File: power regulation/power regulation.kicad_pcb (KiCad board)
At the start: 4 copper layers, 200 x 100 mm, 89 parts, among them J1 Conn_01x02_Pin, J2 Conn_01x02_Pin, J3 Conn_01x02_Pin, M1 TO-236AB_SOT23_NEX, M2 TO-236AB_SOT23_NEX, U1 LT8640SEV_PBF, U2 LT8640SEV_PBF, U3 LT8619EDD-TRPBF

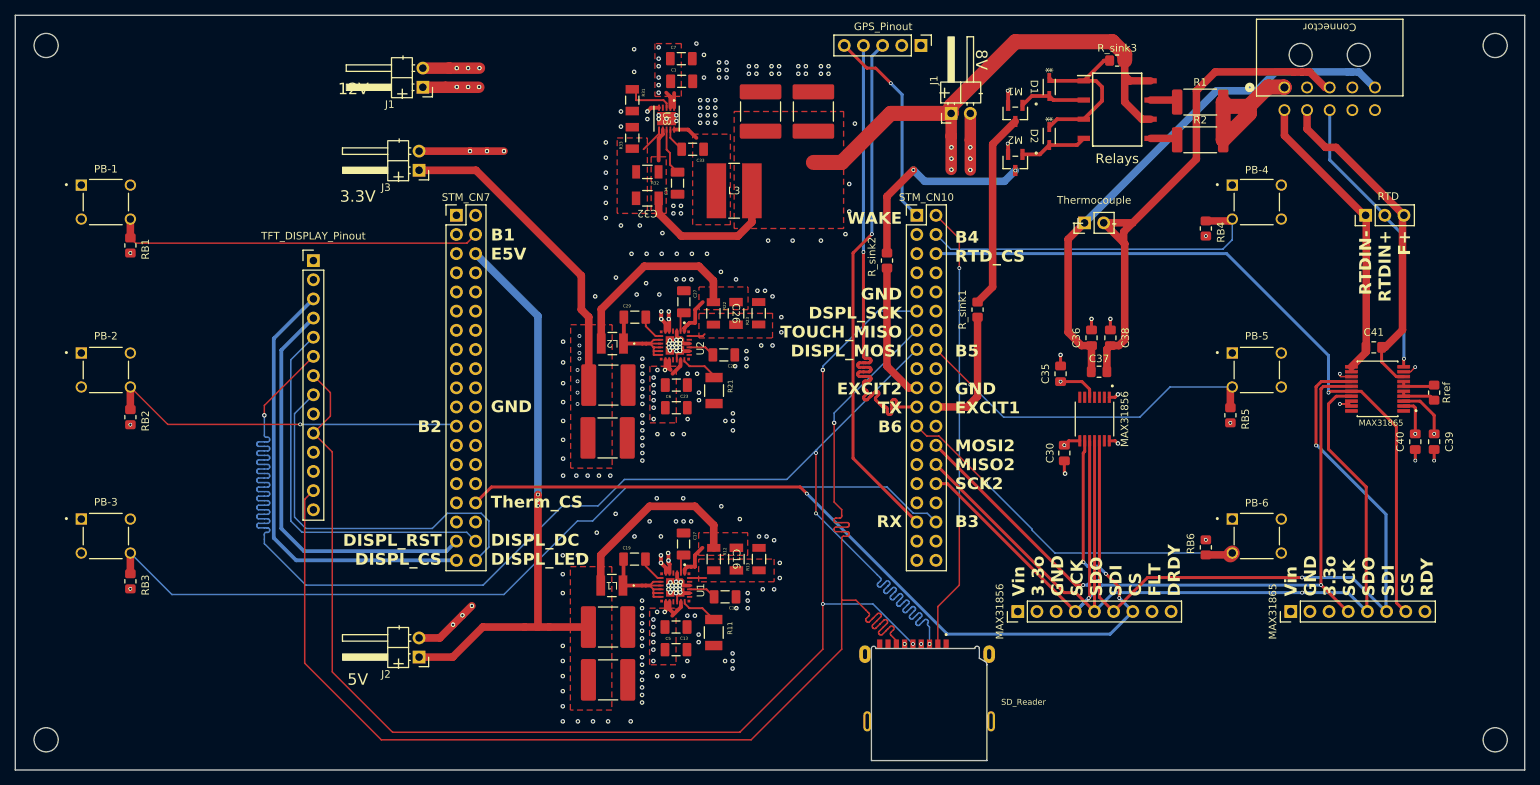
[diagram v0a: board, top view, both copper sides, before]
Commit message: resize button spacing for screen and moved screen headers to center.
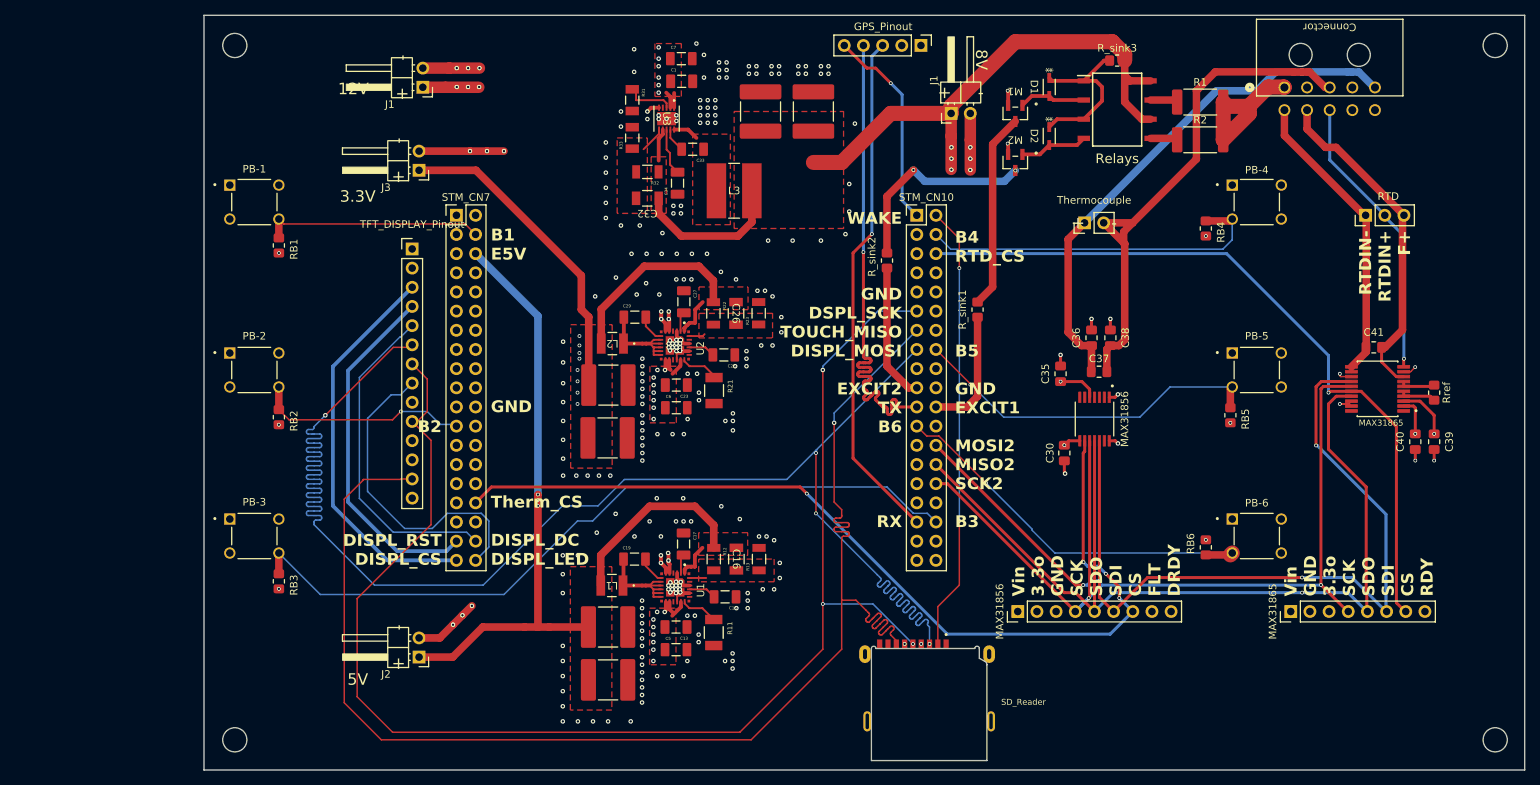
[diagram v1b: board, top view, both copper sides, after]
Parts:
- moved REF** 25.0 mm to (73.5, 138.0)
- moved REF** 25.0 mm to (73.5, 46.0)
- moved PB-1 19.7 mm to (76.1, 66.8)
- moved PB-2 19.7 mm to (76.1, 89.0)
- moved PB-3 19.7 mm to (76.1, 111.0)
- moved RB1 19.7 mm to (79.3, 72.5)
- moved RB2 19.7 mm to (79.3, 95.2)
- moved RB3 19.7 mm to (79.3, 117.0)
- moved TFT_DISPLAY_Pinout 13.2 mm to (97.0, 73.0)
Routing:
- net B2: track 48.3 -> 28.3 mm
- net B3: track 119.6 -> 99.9 mm
- net B1: track 49.0 -> 29.4 mm
- net DISPL_LED: track 50.8 -> 42.8 mm
- net DISPL_RST: track 54.6 -> 47.0 mm
- net DISPL_DC: track 51.2 -> 43.6 mm
- net DISPL_CS: track 59.3 -> 52.7 mm
- net TOUCH_MISO: track 178.1 -> 184.4 mm
- net DISPL_SCK: track 182.1 -> 186.6 mm
- net DISPL_MOSI: track 208.6 -> 210.9 mm
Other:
- board size 200 x 100 mm -> 175 x 100 mm

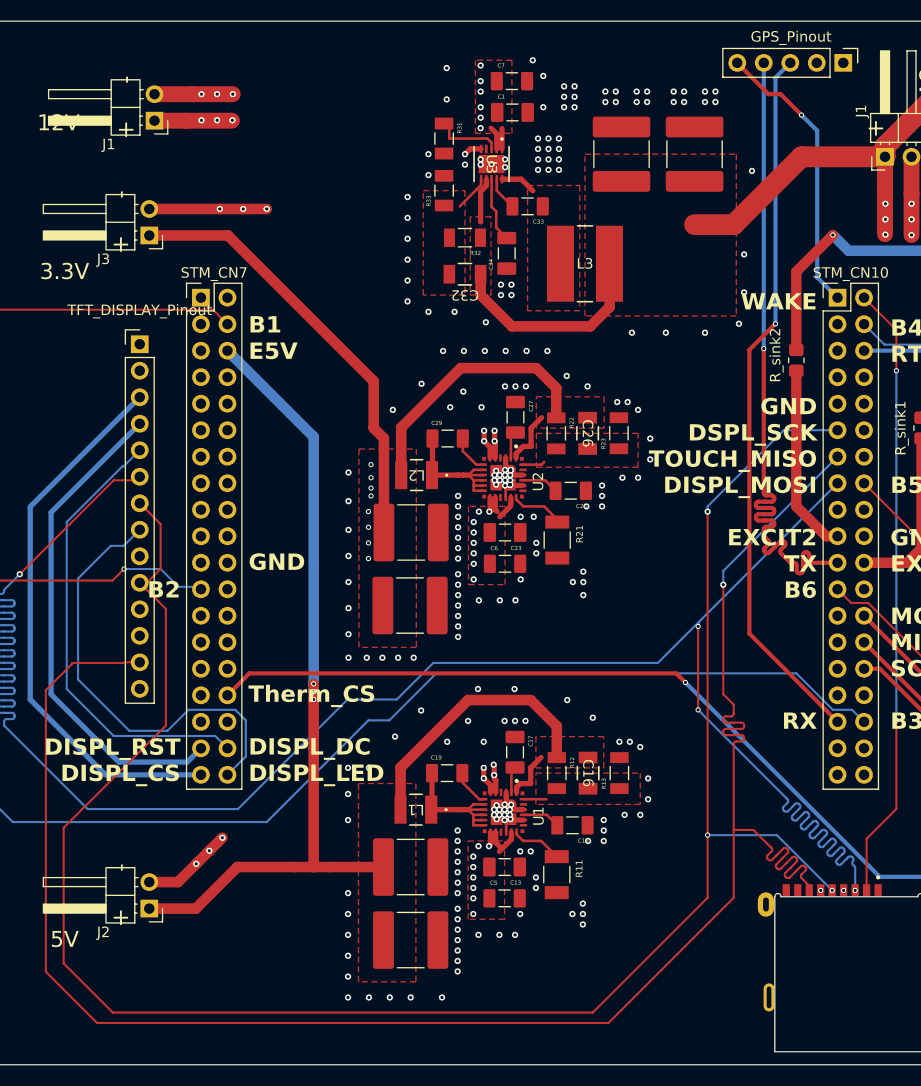
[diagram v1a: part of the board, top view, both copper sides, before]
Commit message: Move GPS headers
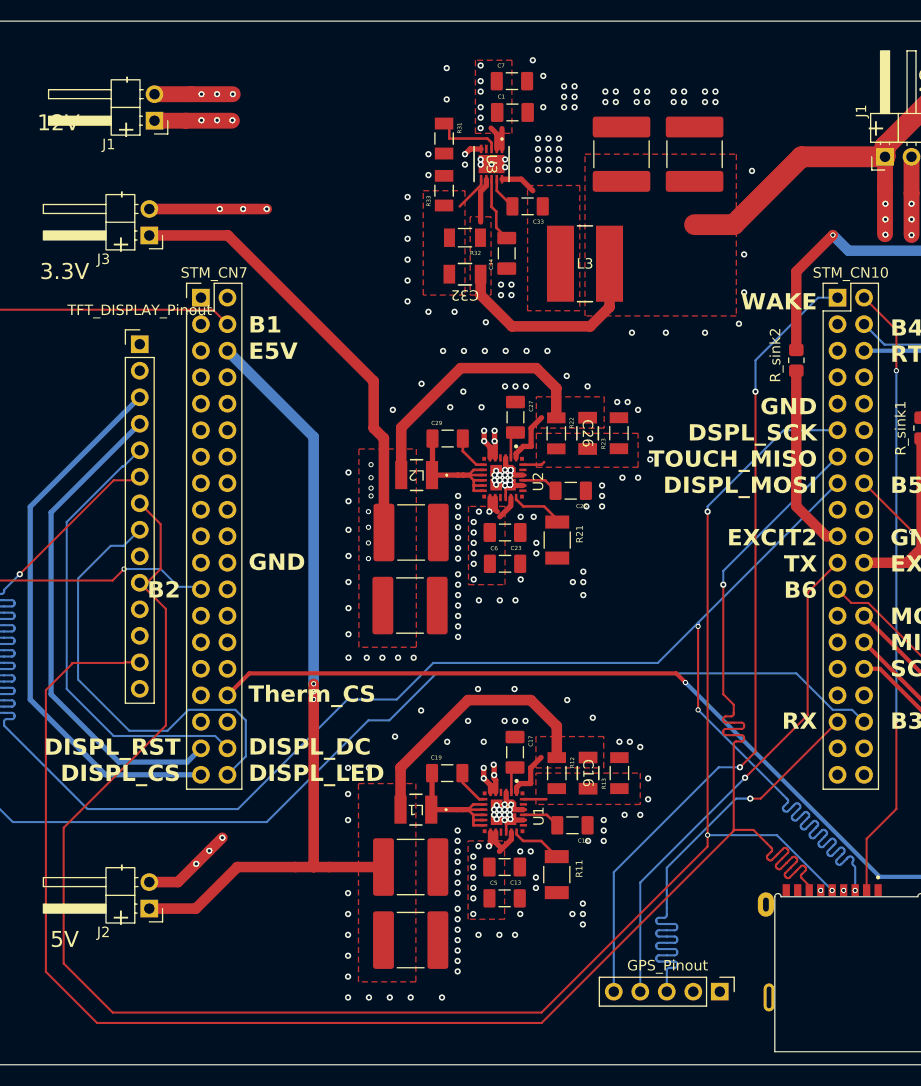
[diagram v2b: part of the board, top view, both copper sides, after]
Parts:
- moved GPS_Pinout 89.8 mm to (152.6, 135.0)
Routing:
- net WAKE: track 27.2 -> 77.7 mm, vias 1 -> 2
- net RX: track 68.3 -> 48.0 mm
- net TX: track 67.8 -> 48.9 mm
- net TOUCH_MISO: track 184.4 -> 180.7 mm
- net DISPL_SCK: track 186.6 -> 183.7 mm
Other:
- board text added: "STM_CN10"
- board text added: "STM_CN7"

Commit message: Add outlines for external MAX modules
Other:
- board text added: "-> STM_Programmer <-"
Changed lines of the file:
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@@
 	)
 	(gr_rect
-		(start 207.4125 70.5)
-		(end 237.4125 125.5)
+		(start 209.5 95)
+		(end 235 123)
 		(stroke
 			(width 0.1)
-			(type default)
-		)
-		(fill no)
-		(layer "B.SilkS")
-	)
-	(gr_rect
-		(start 173.9125 71.5)
-		(end 200.9125 126)
+			(type solid)
+		)
+		(fill no)
+		(layer "B.SilkS")
+	)
+	(gr_rect
+		(start 175 101)
+		(end 200 123)
 		(stroke
 			(width 0.1)
-			(type default)
+			(type solid)
 		)
 		(fill no)
@@
 		)
 	)
+	(gr_text "-> STM_Programmer <-"
+		(at 133.5 55.5 0)
+		(layer "B.SilkS")
+		(effects
+			(font
+				(size 2 2)
+				(thickness 0.25)
+			)
+			(justify bottom mirror)
+		)
+	)
 	(gr_text "Vin\nGND\n3.3o\nSCK\nSDO\nSDI\nCS\nRDY"
 		(at 232.4125 119 90)
@@
 	)
 	(gr_text "MAX31865"
-		(at 210.9125 121 90)
+		(at 208.5 119 90)
 		(layer "B.SilkS")
 		(effects
@@
 	)
 	(gr_text "MAX31856"
-		(at 174.9125 121 90)
-		(layer "B.SilkS")
-		(effects
+		(at 174 119.5 90)
+		(layer "B.SilkS")
+		(effects

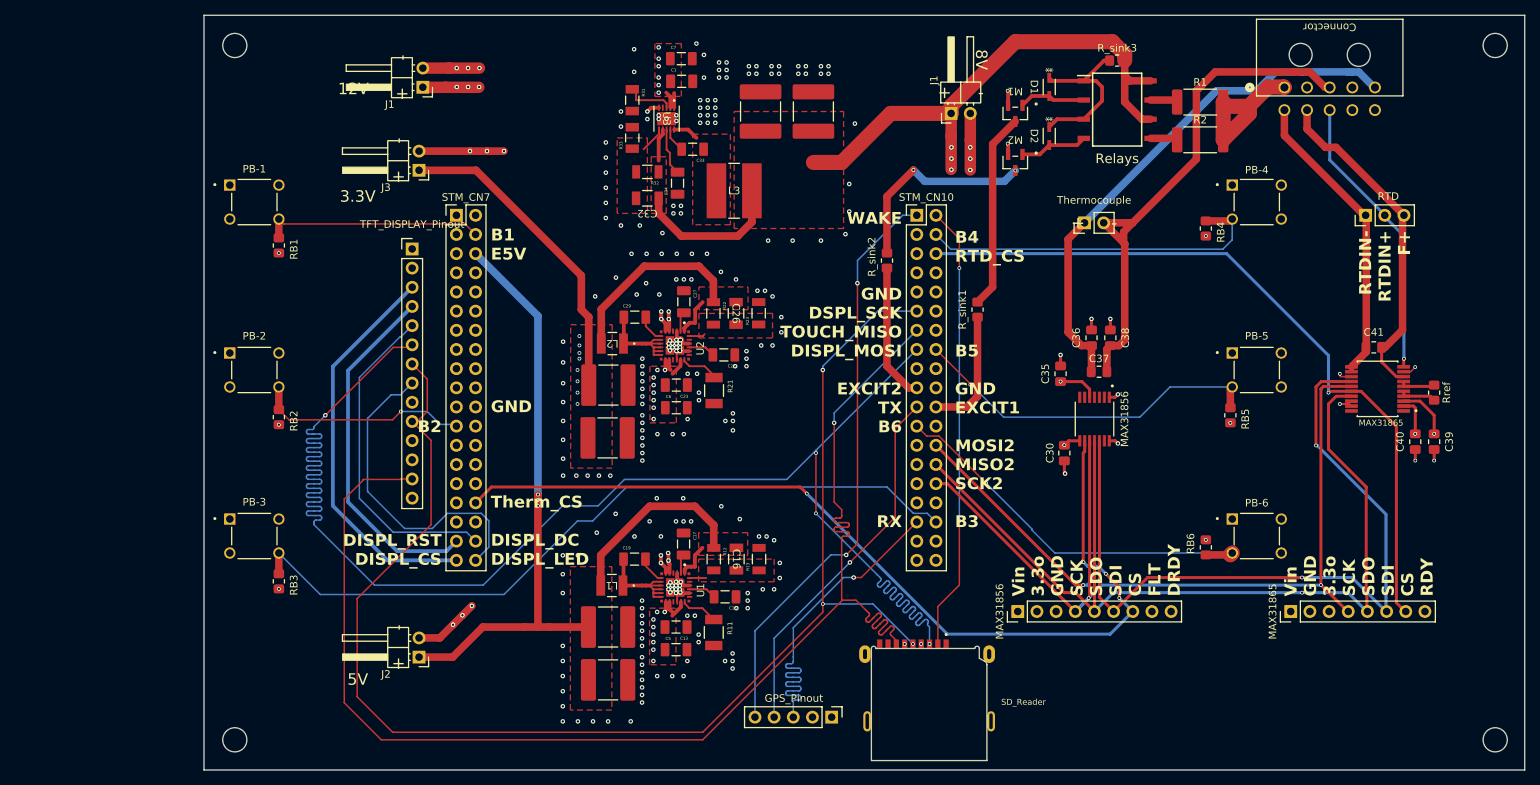
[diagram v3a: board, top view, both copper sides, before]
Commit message: Flip Maxx modules so they can be mounted upsidown on the bottom of the board. I also made some changes to silk screens and vias to remove a bunch of wranings.
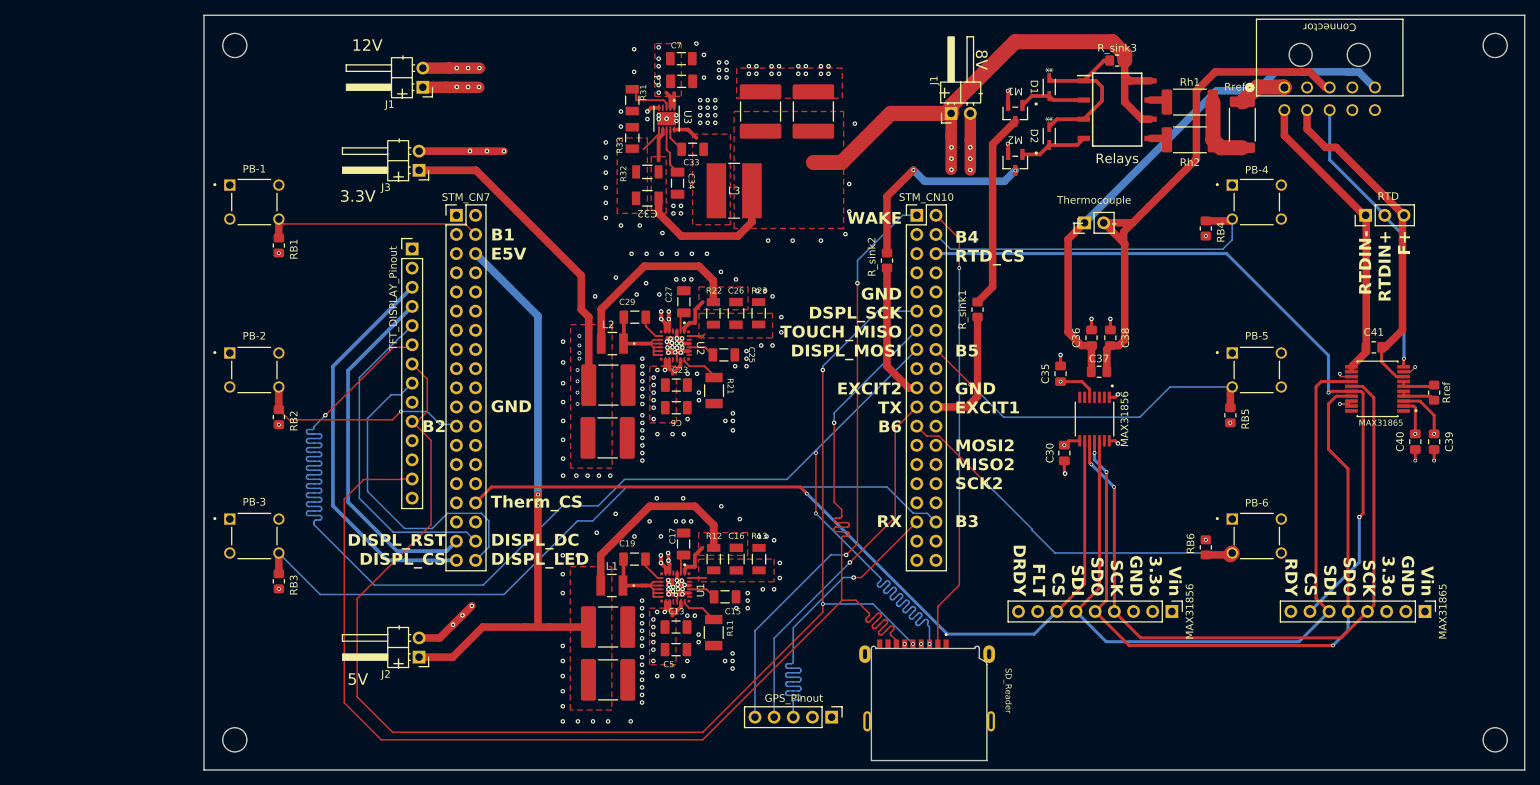
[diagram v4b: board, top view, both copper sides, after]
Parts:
- added Rref: R_2512_6332Metric_Pad1.40x3.35mm_HandSolder, Resistor_SMD:R_2512_6332Metric_Pad1.40x3.35mm_HandSolder, F.Cu at (207.0, 56.5)
- moved MAX31856 20.4 mm to (197.7, 121.0), turned to -90 degrees
- moved MAX31865 17.8 mm to (231.2, 121.0), turned to -90 degrees
- moved Rh1 1.36 mm to (200.1, 53.5)
- moved Rh2 1.36 mm to (200.1, 58.5)
- renumbered R1 to Rh1, R2 to Rh2
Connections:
- Rh1 pad 2: Heater+ -> HeaterPre
- Rh2 pad 2: Heater+ -> HeaterPre
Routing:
- net MAX_SDI: track 131.5 -> 96.2 mm, vias 4 -> 0
- net MAX_SDO: track 122.9 -> 94.7 mm, vias 2 -> 3
- net MAX_SCK: track 118.1 -> 92.7 mm
- net Heater+: track 20.5 -> 6.41 mm
- net Therm_CS: track 123.6 -> 111.4 mm, vias 4 -> 1
- net HeaterPre: track 0.00 -> 9.33 mm
- net SSRout-2: track 3.60 -> 2.24 mm
- net SSRout-1: track 3.64 -> 2.27 mm
- net RTD_CS: track 98.5 -> 99.1 mm, vias 1 -> 2
- net GND: track 69.0 -> 69.1 mm, vias 256 -> 250

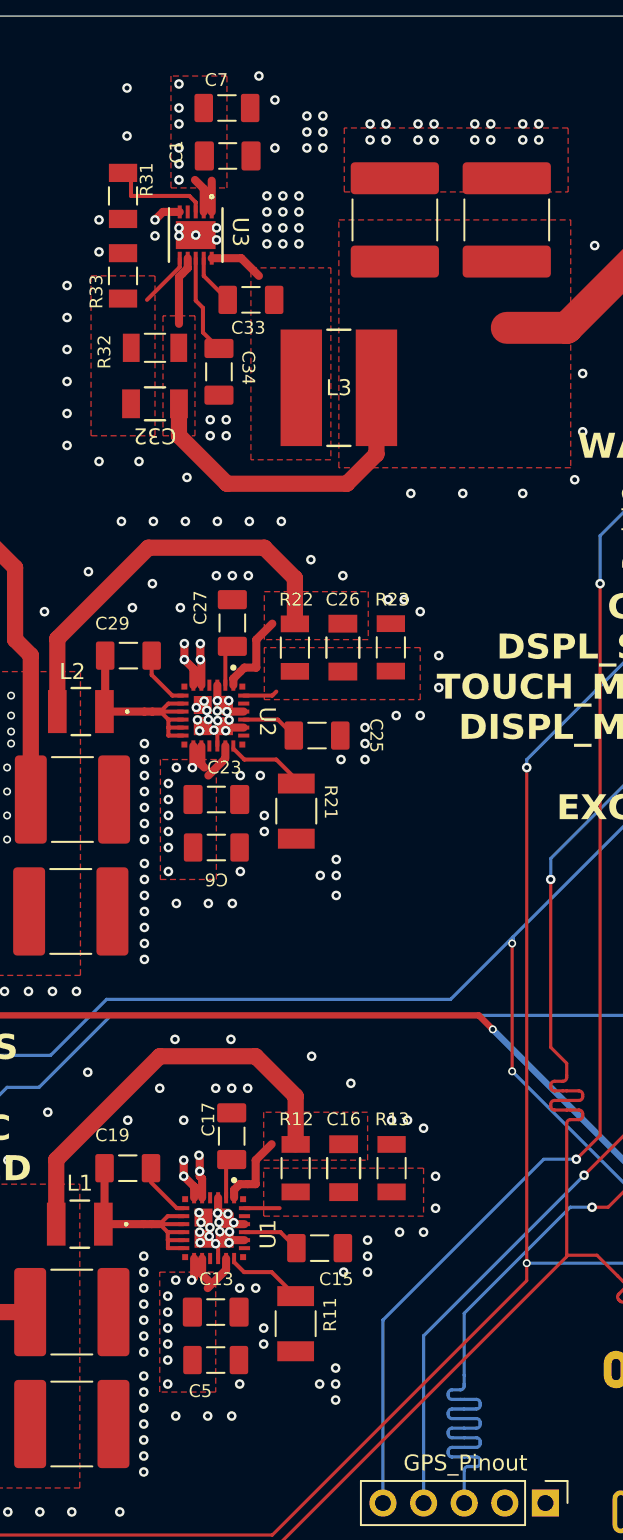
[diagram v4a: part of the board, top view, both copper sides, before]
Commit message: Add Marc's changes the connect components to ground.
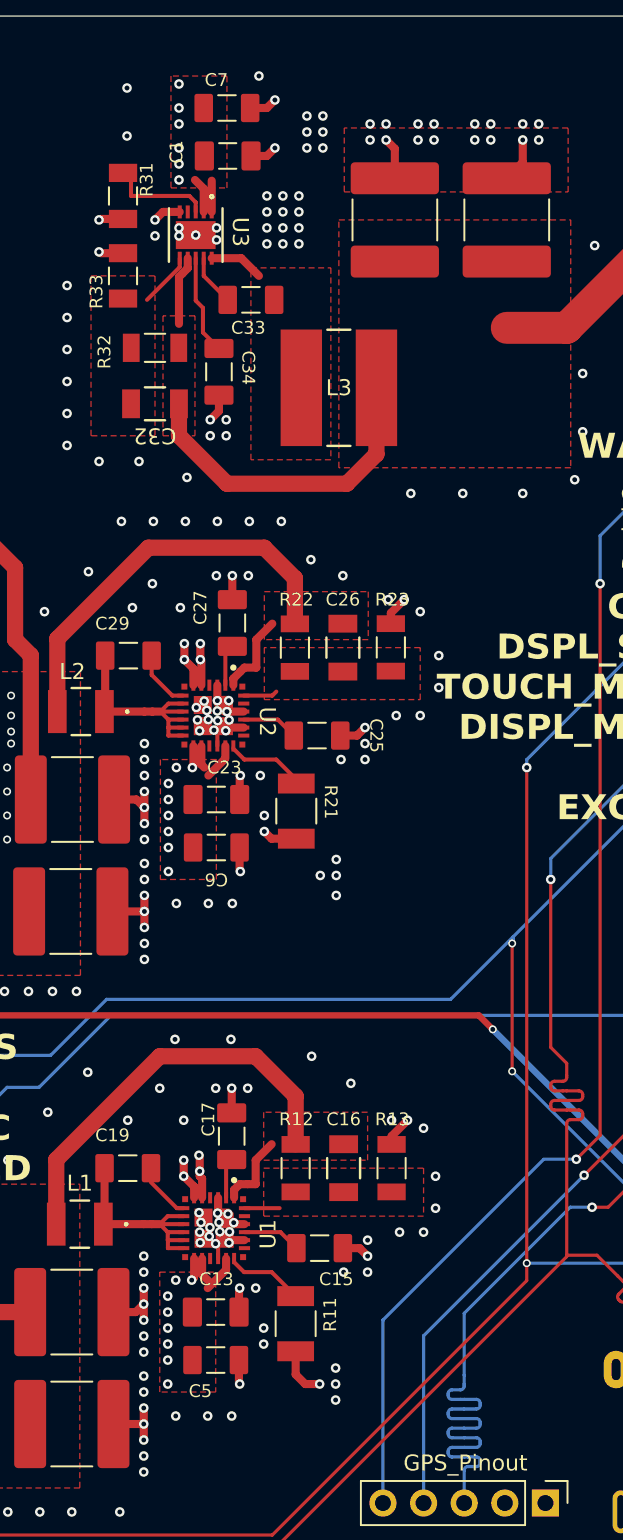
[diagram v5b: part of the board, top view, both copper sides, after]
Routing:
- net GND: track 69.1 -> 120.7 mm
